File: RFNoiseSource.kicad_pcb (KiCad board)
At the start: 2 copper layers, 70 x 31 mm, 46 parts, among them J1 Barrel_Jack, J2 Conn_Coaxial, J3 Conn_Coaxial, Q1 2SC3356, Q2 2SC3356, Q3 2SC3356, Q4 2SC3356, Q5 2SC3356, Q6 2SC3356, U1 AMS1117-3V3

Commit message: Added LCSC part numbers, added cutout notched, added series base resistors to emitter followers
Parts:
- added C14: 10 nF, Capacitors_SMD:C_0805_HandSoldering, F.Cu at (143.6, 86.8)
- added C15: 10 nF, Capacitors_SMD:C_0805_HandSoldering, F.Cu at (156.7, 98.0)
- added C16: 10 nF, Capacitors_SMD:C_0805_HandSoldering, F.Cu at (125.1, 98.3)
- added R19: NC, Resistors_SMD:R_0805_HandSoldering, F.Cu at (175.0, 91.1)
- added R20: 0R, Resistors_SMD:R_0805_HandSoldering, F.Cu at (176.5, 85.9)
- added R21: NC, Resistors_SMD:R_0805_HandSoldering, F.Cu at (177.7, 82.5)
- added R22: NC, Resistors_SMD:R_0805_HandSoldering, F.Cu at (174.2, 105.4)
- added R23: 0R, Resistors_SMD:R_0805_HandSoldering, F.Cu at (176.4, 102.0)
- added R24: NC, Resistors_SMD:R_0805_HandSoldering, F.Cu at (177.6, 105.5)
- added R25: 220R, Resistors_SMD:R_0805_HandSoldering, F.Cu at (150.5, 85.2)
- added R26: 220R, Resistors_SMD:R_0805_HandSoldering, F.Cu at (167.6, 91.5)
- added R27: 220R, Resistors_SMD:R_0805_HandSoldering, F.Cu at (166.2, 100.5)
- R1: value 1k -> 2k2
- R12, R4: value 10k -> 1k
- moved R13 6.37 mm to (165.8, 106.5), turned to 180 degrees
- moved R16 6.28 mm to (154.2, 85.7), turned to 270 degrees
- moved R8 5.51 mm to (157.8, 93.3), turned to 0 degrees
- moved R18 5.40 mm to (152.2, 91.2), turned to 0 degrees
- moved C12 4.13 mm to (149.0, 88.2)
- moved C11 4.05 mm to (171.8, 102.0)
- moved R17 3.35 mm to (145.6, 86.8)
- moved R11 3.25 mm to (172.6, 84.2), turned to 90 degrees
- moved R9 3.14 mm to (169.7, 89.7), turned to 0 degrees
- moved C4 3.08 mm to (155.6, 89.1), turned to 180 degrees
- moved C6 2.96 mm to (165.1, 89.7)
- moved C8 2.93 mm to (173.7, 87.7)
- moved Q3 2.74 mm to (169.4, 86.9), turned to 90 degrees
- moved R15 2.71 mm to (168.9, 105.0), turned to 270 degrees
- moved Q6 2.55 mm to (151.5, 88.3), turned to 0 degrees
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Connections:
- J2 pad 1: Net-(C8-Pad1) -> Net-(J2-Pad1)
- J3 pad 1: Net-(C11-Pad1) -> Net-(J3-Pad1)
- Q3 pad 1: Net-(C6-Pad1) -> Net-(Q3-Pad1)
- Q5 pad 1: Net-(C9-Pad1) -> Net-(Q5-Pad1)
- Q6 pad 1: Net-(C12-Pad1) -> Net-(Q6-Pad1)
- R13 pad 1: Net-(C9-Pad1) -> Net-(Q5-Pad1)
- R16 pad 1: Net-(C12-Pad1) -> Net-(Q6-Pad1)
- R9 pad 1: Net-(C6-Pad1) -> Net-(Q3-Pad1)
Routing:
- net GND: track 222.2 -> 239.2 mm, vias 100 -> 111
- net Net-(Q5-Pad1): track 0.00 -> 8.59 mm
- net Net-(C6-Pad1): track 8.96 -> 1.93 mm
- net Net-(J2-Pad1): track 0.00 -> 6.74 mm
- net Net-(C16-Pad2): track 118.3 -> 124.8 mm
- net Net-(J3-Pad1): track 0.00 -> 6.45 mm
- net Net-(Q6-Pad1): track 0.00 -> 5.36 mm
- net Net-(C12-Pad2): track 9.30 -> 4.08 mm
- net Net-(Q3-Pad1): track 0.00 -> 4.49 mm
- net Net-(C10-Pad2): track 12.2 -> 7.97 mm
- net Net-(C6-Pad2): track 12.9 -> 9.04 mm
- net Net-(C12-Pad1): track 5.02 -> 1.81 mm
- net Net-(C9-Pad1): track 5.02 -> 2.43 mm
- net Net-(C11-Pad1): track 6.79 -> 5.01 mm
- net Net-(C11-Pad2): track 7.35 -> 5.61 mm
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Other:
- board text removed: "BROADBAND NOISE GENERATOR BY D. MARKS KW4TI CC-BY-SA 4.0"

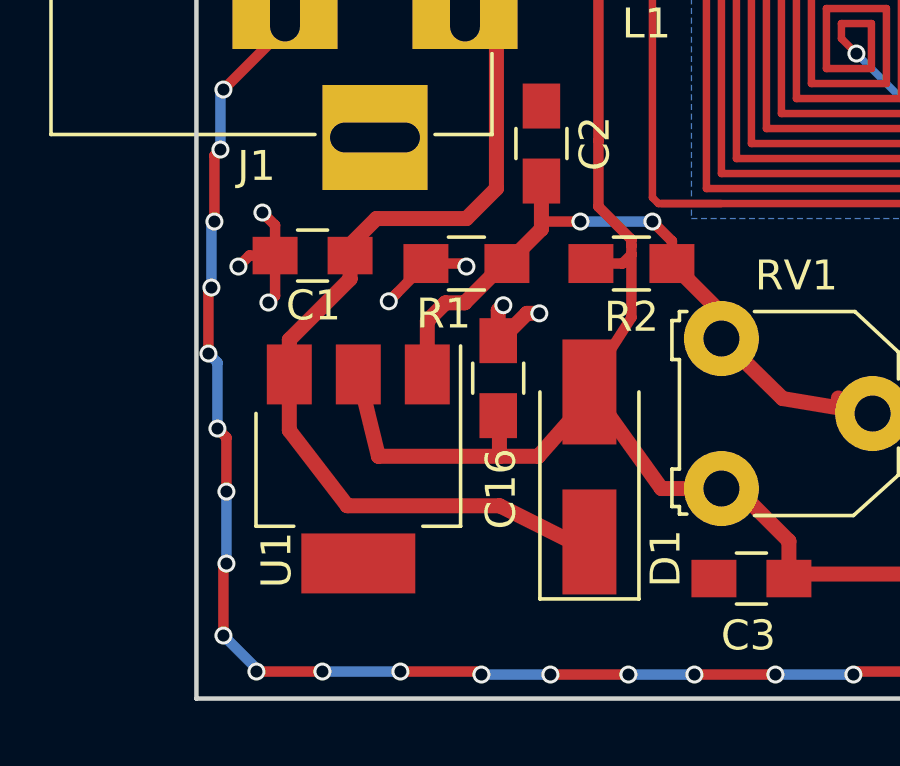
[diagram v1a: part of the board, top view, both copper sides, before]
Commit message: Changed regulator
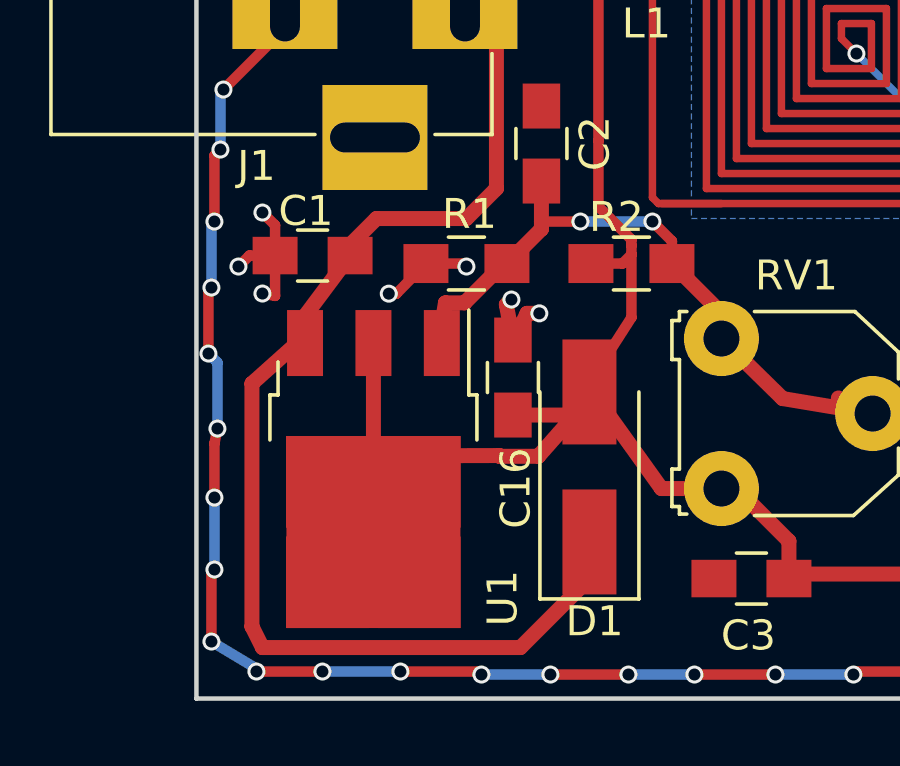
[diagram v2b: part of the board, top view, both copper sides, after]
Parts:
- U1: value AMS1117-3V3 -> LM317MDT; footprint TO_SOT_Packages_SMD:SOT-223 -> TO_SOT_Packages_SMD:TO-252-3_TabPin2
- moved U1 0.50 mm to (120.9, 101.3)
- moved C16 0.49 mm to (125.5, 98.3)
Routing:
- net Net-(C1-Pad2): track 31.1 -> 40.5 mm
- net Net-(C16-Pad2): track 124.8 -> 131.1 mm
- net Net-(C2-Pad2): track 24.4 -> 22.4 mm
